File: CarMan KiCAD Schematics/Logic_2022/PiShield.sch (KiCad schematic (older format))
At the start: 13 parts, among them J2 J2 NI I2C, J4 J4 GLV BOB, U10 BNO_055, U11 Raspberry_Pi_RTC, U6 RaspberryPi3

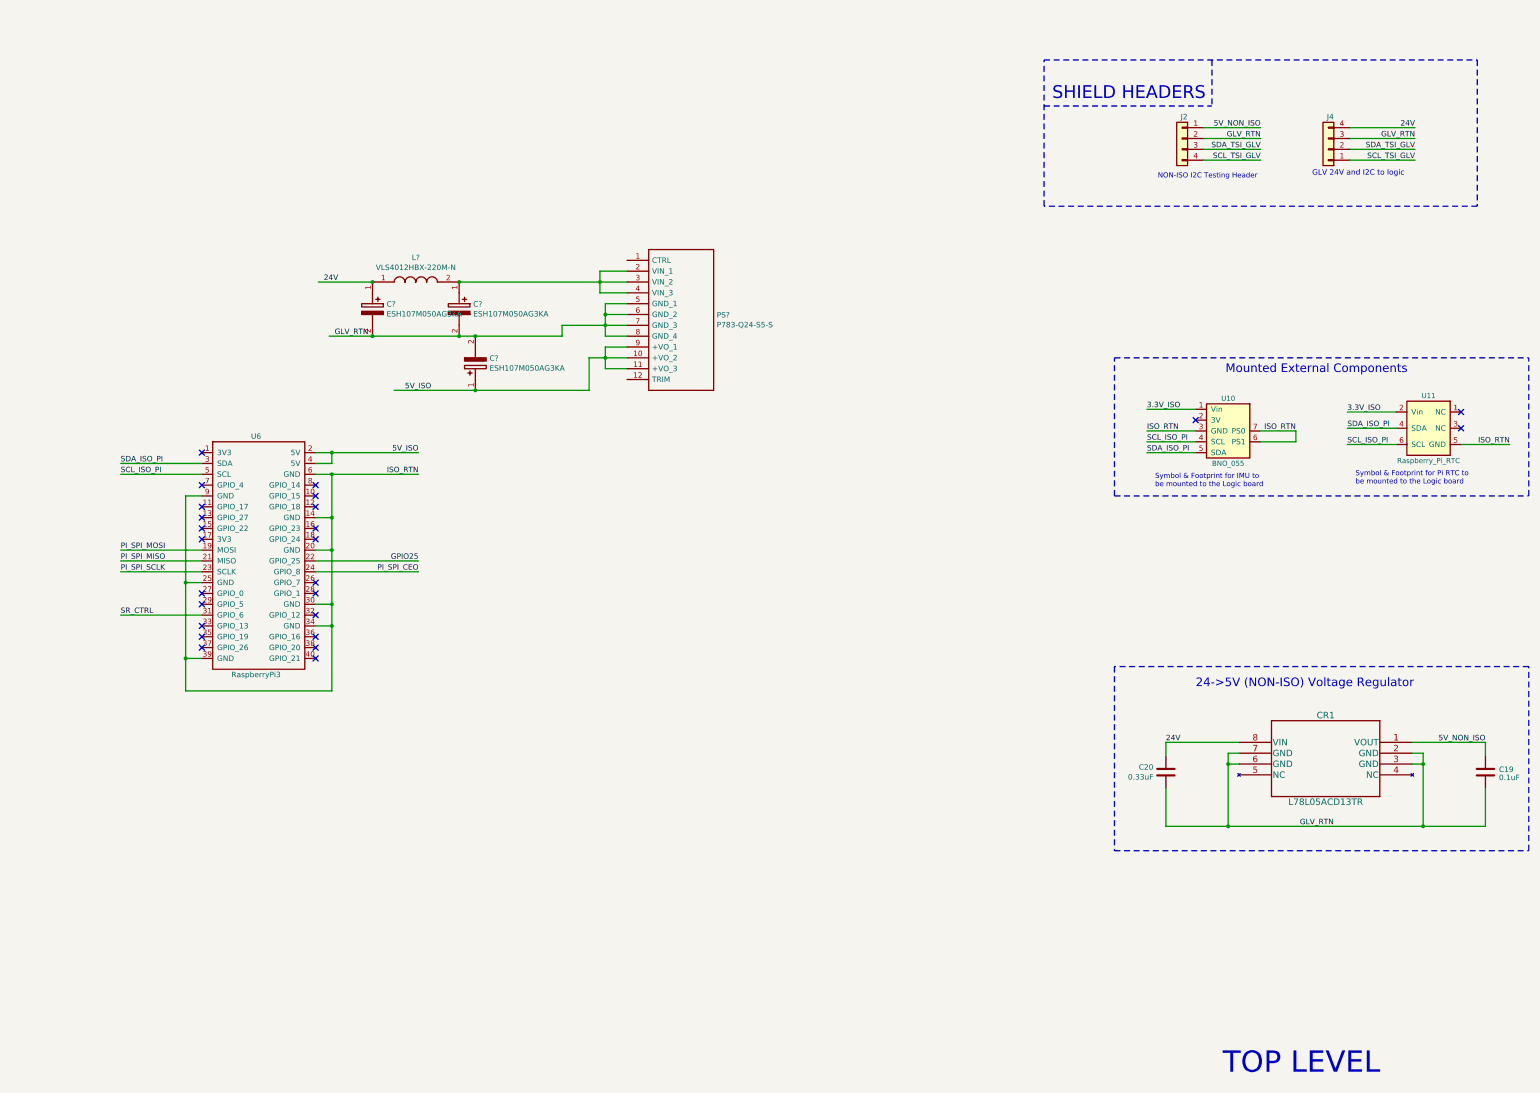
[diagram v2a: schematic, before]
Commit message: Added the Pi shield components as well as the footprints needed
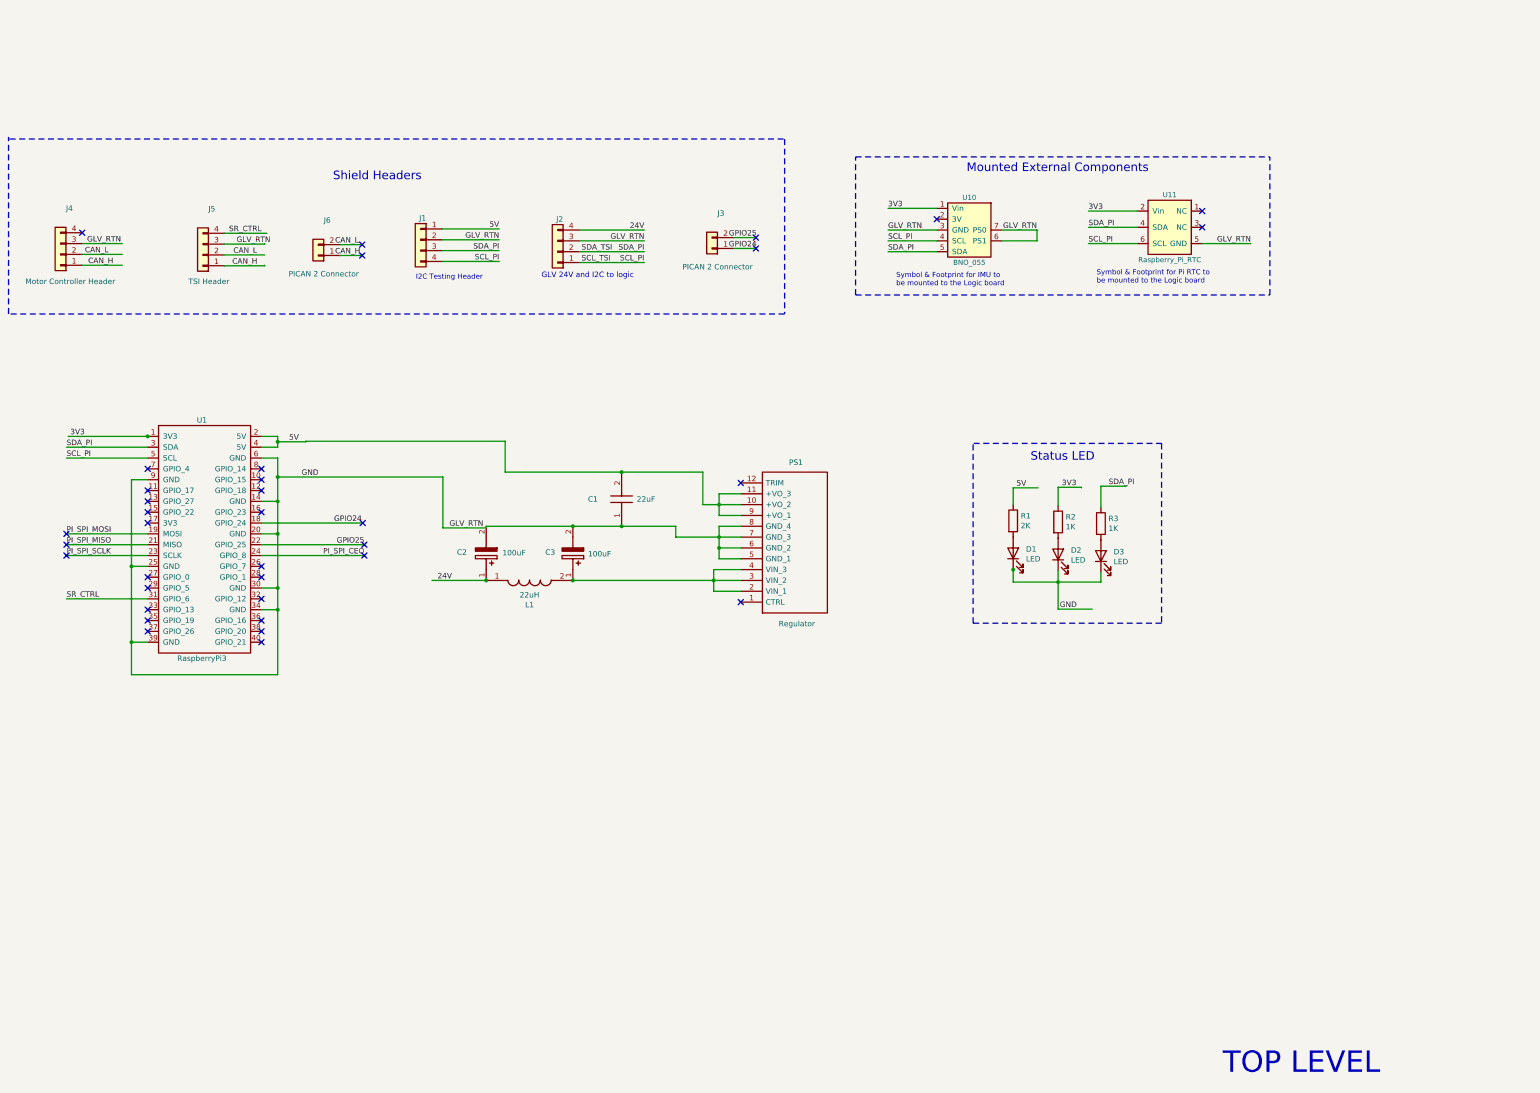
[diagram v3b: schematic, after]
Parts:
- removed C19: 0.1uF, Capacitor_SMD:C_0805_2012Metric_Pad1.15x1.40mm_HandSolder, symbol Device:C
- removed C20: 0.33uF, Capacitor_SMD:C_0805_2012Metric_Pad1.15x1.40mm_HandSolder, symbol Device:C
- removed C?: ESH107M050AG3KA, CAPPRD350W60D800H1250, symbol SamacSys_Parts:ESH107M050AG3KA
- removed CR1: L78L05ACD13TR, CarMan General Footprints:L78L05ACD13TR, symbol Logic-rescue:L78L05ACD13TR-CarMan_KiCAD_Library
- added C1: 22uF, CAPC3216X180N, symbol SamacSys_Parts:LMJ316BB7226KLHT
- added D1, D2, D3: LED, CarMan General Footprints:VAOL-S8GT4, symbol Device:LED
- added J3, J6: PICAN 2 Connector, Connector_PinHeader_2.54mm:PinHeader_1x02_P2.54mm_Vertical, symbol Connector_Generic:Conn_01x02
- added J4: Motor Controller Header, CarMan General Footprints:Molex_MiniFit-JR-5556-04A_2x02x4.20mm_Straight, symbol Logic-rescue:Conn_01x04-Connector_Generic-Logic-rescue
- added J5: TSI Header, Connector_PinHeader_2.54mm:PinHeader_2x05_P2.54mm_Vertical, symbol Logic-rescue:Conn_01x04-Connector_Generic-Logic-rescue
- added R1: 2K, Resistor_SMD:R_0805_2012Metric_Pad1.20x1.40mm_HandSolder, symbol Device:R
- added R2, R3: 1K, Resistor_SMD:R_0805_2012Metric_Pad1.20x1.40mm_HandSolder, symbol Device:R
- C2, C3: renamed from C?; value ESH107M050AG3KA -> 100uF
- L1: renamed from L?; value VLS4012HBX-220M-N -> 22uH
- PS1: renamed from PS?; value P783-Q24-S5-S -> Regulator
- renumbered J2 to J1, J4 to J2, U6 to U1
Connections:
- net labels added: 3V3, 5V, CAN_H, CAN_L, GND, GPIO24, SCL_PI, SCL_TSI, SDA_PI, SDA_TSI
- net labels removed: 3.3V_ISO, 5V_ISO, 5V_NON_ISO, ISO_RTN, SCL_ISO_PI, SCL_TSI_GLV, SDA_ISO_PI, SDA_TSI_GLV
- wire segments 95 -> 117
- no-connect marks 25 -> 36
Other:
- note added: "I2C Testing Header"
- note added: "Shield Headers"
- note added: "Status LED"
- note removed: "24->5V (NON-ISO) Voltage Regulator"
- note removed: "NON-ISO I2C Testing Header"
- note removed: "SHIELD HEADERS"
- moved on the sheet: C2, C3, J1, J2, L1, PS1, U1, U10, U11

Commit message: Created the PCB layout of the Pi shield
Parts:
- C1: footprint CAPC3216X180N -> SamacSys_Parts:CAPC3216X180N
- C2, C3: footprint CAPPRD350W60D800H1250 -> SamacSys_Parts:CAPPRD350W60D800H1250
- L1: footprint VLS4012HBX220MN -> SamacSys_Parts:VLS4012HBX220MN
- PS1: footprint P783Q24S5S -> SamacSys_Parts:P783Q24S5S
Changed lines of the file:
@@
 F 0 "PS1" H 9145 4715 50  0000 L CNN
 F 1 "Regulator" H 9050 6205 50  0000 L CNN
-F 2 "P783Q24S5S" H 9550 6105 50  0001 L CNN
+F 2 "SamacSys_Parts:P783Q24S5S" H 9550 6105 50  0001 L CNN
 F 3 "https://www.cui.com/product/resource/digikeypdf/p783-s.pdf" H 9550 6005 50  0001 L CNN
 F 4 "Non-Isolated DC/DC Converters 5 Vdc, 3 A, 15 W, 8~36 Vdc Input Range" H 9550 5905 50  0001 L CNN "Description"
@@
 F 0 "C3" V 7410 5550 50  0000 L CNN
 F 1 "100uF" V 7395 5945 50  0000 L CNN
-F 2 "CAPPRD350W60D800H1250" H 7500 5855 50  0001 L CNN
+F 2 "SamacSys_Parts:CAPPRD350W60D800H1250" H 7500 5855 50  0001 L CNN
 F 3 "https://connect.kemet.com:7667/gateway/IntelliData-ComponentDocumentation/1.0/download/specsheet/ESH107M050AG3KA" H 7500 5755 50  0001 L CNN
 F 4 "ESH, Aluminum Electrolytic, 100 uF, 20%, 50 VDC, -40/+105C, Lead Spacing = 3.5mm" H 7500 5655 50  0001 L CNN "Description"
@@
 F 0 "L1" H 6750 6030 50  0000 C CNN
 F 1 "22uH" H 6750 5939 50  0000 C CNN
-F 2 "VLS4012HBX220MN" H 7000 5855 50  0001 L CNN
+F 2 "SamacSys_Parts:VLS4012HBX220MN" H 7000 5855 50  0001 L CNN
 F 3 "https://product.tdk.com/system/files/dam/doc/product/inductor/inductor/smd/catalog/inductor_commercial_power_vls4012hbx-n_en.pdf" H 7000 5755 50  0001 L CNN
 F 4 "SMD / SMT Inductors (Coils), L=22?H, L x W x T :" H 7000 5655 50  0001 L CNN "Description"
@@
 F 0 "C2" V 6610 5535 50  0000 L CNN
 F 1 "100uF" V 6605 5955 50  0000 L CNN
-F 2 "CAPPRD350W60D800H1250" H 6700 5855 50  0001 L CNN
+F 2 "SamacSys_Parts:CAPPRD350W60D800H1250" H 6700 5855 50  0001 L CNN
 F 3 "https://connect.kemet.com:7667/gateway/IntelliData-ComponentDocumentation/1.0/download/specsheet/ESH107M050AG3KA" H 6700 5755 50  0001 L CNN
 F 4 "ESH, Aluminum Electrolytic, 100 uF, 20%, 50 VDC, -40/+105C, Lead Spacing = 3.5mm" H 6700 5655 50  0001 L CNN "Description"
@@
 F 0 "C1" V 7850 5570 50  0000 C CNN
 F 1 "22uF" V 7850 5080 50  0000 C CNN
-F 2 "CAPC3216X180N" H 7950 5355 50  0001 L CNN
+F 2 "SamacSys_Parts:CAPC3216X180N" H 7950 5355 50  0001 L CNN
 F 3 "https://ds.yuden.co.jp/TYCOMPAS/ut/detail?pn=LMJ316BB7226KLHT  &u=M" H 7950 5255 50  0001 L CNN
 F 4 "Taiyo Yuden LMJ316BB7226KLHT 22F MLCC 10V dc +/-10% Tolerance SMD" H 7950 5155 50  0001 L CNN "Description"

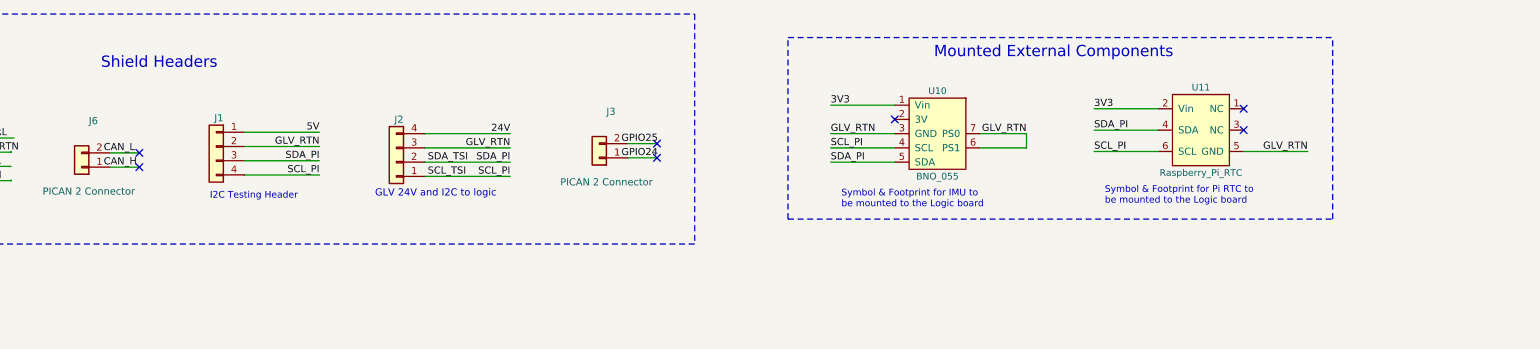
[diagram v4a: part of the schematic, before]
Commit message: Update the PCB layout with the wiring connected
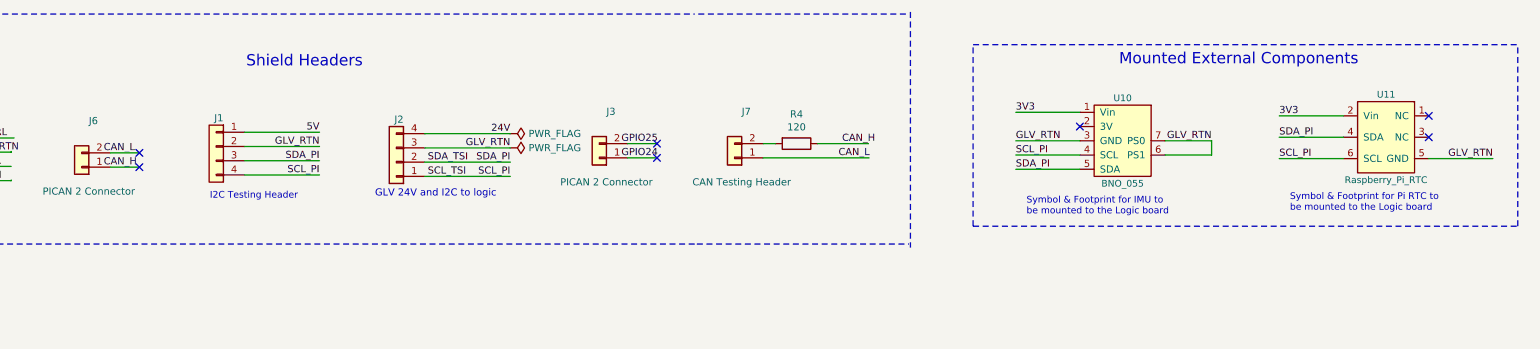
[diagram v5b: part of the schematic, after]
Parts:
- added F1, F2: PWR_FLAG, symbol power:PWR_FLAG
- added J7: CAN Testing Header, Connector_PinHeader_2.54mm:PinHeader_1x02_P2.54mm_Vertical, symbol Connector_Generic:Conn_01x02
- added R4: 120, Resistor_SMD:R_0805_2012Metric_Pad1.20x1.40mm_HandSolder, symbol Logic-rescue:R-Device-Logic-rescue
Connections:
- wire segments 117 -> 120
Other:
- moved on the sheet: U10, U11
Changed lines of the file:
@@
 NoConn ~ 4275 5175
-Wire Wire Line
-	7210 2570 7810 2570
 Wire Wire Line
 	7810 2670 7210 2670
@@
 L Logic-rescue:Raspberry_Pi_RTC-CarMan_KiCAD_Library U11
 U 1 1 60875061
-P 12660 2545
-F 0 "U11" H 12660 2845 47  0000 C CNN
-F 1 "Raspberry_Pi_RTC" H 12660 2245 47  0000 C CNN
-F 2 "CarMan General Footprints:Raspberry_Pi_RTC" V 12660 2545 47  0001 C CNN
-F 3 "" V 12660 2545 47  0001 C CNN
-F 4 "U11 - Pi RTC" H 12660 2545 50  0001 C CNN "Board Label"
-	1    12660 2545
+P 13960 2595
+F 0 "U11" H 13960 2895 47  0000 C CNN
+F 1 "Raspberry_Pi_RTC" H 13960 2295 47  0000 C CNN
+F 2 "CarMan General Footprints:Raspberry_Pi_RTC" V 13960 2595 47  0001 C CNN
+F 3 "" V 13960 2595 47  0001 C CNN
+F 4 "U11 - Pi RTC" H 13960 2595 50  0001 C CNN "Board Label"
+	1    13960 2595
 	1    0    0    -1
 $EndComp
-Text Notes 11985 3070 0    47   ~ 0
+Text Notes 13285 3120 0    47   ~ 0
 Symbol & Footprint for Pi RTC to\nbe mounted to the Logic board
-NoConn ~ 12960 2395
-NoConn ~ 12960 2545
-Text Notes 10135 3095 0    47   ~ 0
+NoConn ~ 14260 2445
+NoConn ~ 14260 2595
+Text Notes 11435 3145 0    47   ~ 0
 Symbol & Footprint for IMU to\nbe mounted to the Logic board
-Text Notes 10785 2045 0    79   ~ 0
+Text Notes 12085 2095 0    79   ~ 0
 Mounted External Components
 Wire Notes Line
-	13585 3170 13585 1895
-Wire Notes Line
-	9760 1895 13585 1895
-Wire Notes Line
-	9760 3170 13585 3170
-Wire Notes Line
-	9760 3170 9760 1895
-NoConn ~ 10510 2470
-Wire Wire Line
-	10510 2370 10060 2370
-Text Label 10060 2370 0    50   ~ 0
+	14885 3220 14885 1945
+Wire Notes Line
+	11060 1945 14885 1945
+Wire Notes Line
+	11060 3220 14885 3220
+Wire Notes Line
+	11060 3220 11060 1945
+NoConn ~ 11810 2520
+Wire Wire Line
+	11810 2420 11360 2420
+Text Label 11360 2420 0    50   ~ 0
 3V3
 $Comp
 L Logic-rescue:BNO_055-CarMan_KiCAD_Library U10
 U 1 1 6081110B
-P 10810 2570
-F 0 "U10" V 10510 2570 47  0000 C CNN
-F 1 "BNO_055" V 11110 2570 47  0000 C CNN
-F 2 "CarMan General Footprints:BNO_055" H 10810 2570 47  0001 C CNN
-F 3 "" H 10810 2570 47  0001 C CNN
-F 4 "U10 - IMU" V 10810 2570 50  0001 C CNN "Board Name"
-	1    10810 2570
+P 12110 2620
+F 0 "U10" V 11810 2620 47  0000 C CNN
+F 1 "BNO_055" V 12410 2620 47  0000 C CNN
+F 2 "CarMan General Footprints:BNO_055" H 12110 2620 47  0001 C CNN
+F 3 "" H 12110 2620 47  0001 C CNN
+F 4 "U10 - IMU" V 12110 2620 50  0001 C CNN "Board Name"
+	1    12110 2620
 	0    1    1    0
 $EndComp
 Wire Wire Line
-	11435 2670 11110 2670
-Wire Wire Line
-	11435 2570 11435 2670
-Wire Wire Line
-	11110 2570 11435 2570
-Wire Wire Line
-	10510 2570 10060 2570
-Text Label 11435 2570 2    50   ~ 0
+	12735 2720 12410 2720
+Wire Wire Line
+	12735 2620 12735 2720
+Wire Wire Line
+	12410 2620 12735 2620
+Wire Wire Line
+	11810 2620 11360 2620
+Text Label 12735 2620 2    50   ~ 0
 GLV_RTN
 Wire Wire Line
-	12360 2545 11910 2545
-Wire Wire Line
-	12360 2695 11910 2695
-Wire Wire Line
-	10510 2770 10060 2770
-Wire Wire Line
-	10510 2670 10060 2670
-Text Label 10060 2570 0    50   ~ 0
+	13660 2595 13210 2595
+Wire Wire Line
+	13660 2745 13210 2745
+Wire Wire Line
+	11810 2820 11360 2820
+Wire Wire Line
+	11810 2720 11360 2720
+Text Label 11360 2620 0    50   ~ 0
 GLV_RTN
-Text Label 10060 2770 0    50   ~ 0
+Text Label 11360 2820 0    50   ~ 0
 SDA_PI
-Text Label 10060 2670 0    50   ~ 0
+Text Label 11360 2720 0    50   ~ 0
 SCL_PI
-Text Label 11910 2545 0    50   ~ 0
+Text Label 13210 2595 0    50   ~ 0
 SDA_PI
-Text Label 11910 2395 0    50   ~ 0
+Text Label 13210 2445 0    50   ~ 0
 3V3
-Text Label 13410 2695 2    50   ~ 0
+Text Label 14710 2745 2    50   ~ 0
 GLV_RTN
-Text Label 11910 2695 0    50   ~ 0
+Text Label 13210 2745 0    50   ~ 0
 SCL_PI
 Wire Wire Line
-	12360 2395 11910 2395
-Wire Wire Line
-	12960 2695 13410 2695
+	13660 2445 13210 2445
+Wire Wire Line
+	14260 2745 14710 2745
 $Comp
 L SamacSys_Parts:P783-Q24-S5-S PS1
@@
 Text Label 4955 2805 0    50   ~ 0
 CAN_H
-Text Notes 4935 2120 0    79   ~ 0
+Text Notes 5955 2110 0    79   ~ 0
 Shield Headers
 NoConn ~ 5205 2705
@@
 	1950 1730 9105 1730
 Wire Notes Line
-	9105 1730 9105 3345
-Wire Notes Line
 	9105 3345 1940 3345
 Wire Notes Line
@@
 NoConn ~ 5225 5475
 NoConn ~ 5210 5275
+$Comp
+L Connector_Generic:Conn_01x02 J7
+U 1 1 6228F919
+P 9385 2740
+F 0 "J7" H 9303 2415 50  0000 C CNN
+F 1 "CAN Testing Header" H 9335 2910 50  0000 C CNN
+F 2 "Connector_PinHeader_2.54mm:PinHeader_1x02_P2.54mm_Vertical" H 9385 2740 50  0001 C CNN
+F 3 "~" H 9385 2740 50  0001 C CNN
+	1    9385 2740
+	-1   0    0    1
+$EndComp
+Wire Wire Line
+	9585 2640 9670 2640
+$Comp
+L Logic-rescue:R-Device-Logic-rescue R4
+U 1 1 622B4E7B
+P 9820 2640
+F 0 "R4" V 9613 2640 50  0000 C CNN
+F 1 "120" V 9704 2640 50  0000 C CNN
+F 2 "Resistor_SMD:R_0805_2012Metric_Pad1.20x1.40mm_HandSolder" V 9750 2640 50  0001 C CNN
+F 3 "" H 9820 2640 50  0001 C CNN
+	1    9820 2640
+	0    1    1    0
+$EndComp
+Wire Wire Line
+	9970 2640 10325 2640
+Wire Wire Line
+	9585 2740 10330 2740
+Text Label 10140 2640 0    50   ~ 0
+CAN_H
+Text Label 10115 2740 0    50   ~ 0
+CAN_L
+Wire Notes Line
+	9130 1730 10610 1730
+Wire Notes Line
+	9120 3345 10610 3345
+Wire Notes Line
+	10620 1715 10620 3370
+$Comp
+L power:PWR_FLAG F1
+U 1 1 62289588
+P 7810 2570
+F 0 "F1" H 7810 2645 50  0001 C CNN
+F 1 "PWR_FLAG" V 7810 2698 50  0000 L CNN
+F 2 "" H 7810 2570 50  0001 C CNN
+F 3 "~" H 7810 2570 50  0001 C CNN
+	1    7810 2570
+	0    1    1    0
+$EndComp
+Wire Wire Line
+	7810 2570 7210 2570
+$Comp
+L power:PWR_FLAG F2
+U 1 1 62298F01
+P 7810 2670
+F 0 "F2" H 7810 2745 50  0001 C CNN
+F 1 "PWR_FLAG" V 7810 2798 50  0000 L CNN
+F 2 "" H 7810 2670 50  0001 C CNN
+F 3 "~" H 7810 2670 50  0001 C CNN
+	1    7810 2670
+	0    1    1    0
+$EndComp
 $EndSCHEMATC
